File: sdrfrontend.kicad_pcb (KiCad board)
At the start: 2 copper layers, 22 parts, among them J1 AudioJack2_Ground, U1 CD4066BE, U2 NJM4580, U3 LM7805_TO220, U5 PIC12F1822-xP

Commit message: make pcb
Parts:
- C1: moved to B.Cu
- R1, R2: footprint Resistor_THT:R_Axial_DIN0207_L6.3mm_D2.5mm_P7.62mm_Horizontal -> Resistor_THT:R_Axial_DIN0207_L6.3mm_D2.5mm_P2.54mm_Vertical
- moved C5 64.6 mm to (165.1, 73.0), turned to -90 degrees
- moved C1 63.5 mm to (154.9, 102.9), turned to 90 degrees
- moved C2 61.7 mm to (162.6, 78.1), turned to -90 degrees
- moved C8 59.3 mm to (157.5, 73.0), turned to 180 degrees
- moved U2 54.2 mm to (152.4, 75.6)
- moved U1 49.0 mm to (152.4, 87.6)
- moved C3 48.8 mm to (149.9, 75.6), turned to -90 degrees
- moved R1 48.8 mm to (165.1, 80.4), turned to 90 degrees
- moved U4 48.0 mm to (142.2, 95.2)
- moved C4 47.0 mm to (147.3, 70.5), turned to -90 degrees
- moved C9 42.1 mm to (142.2, 85.7), turned to -90 degrees
- moved U5 35.9 mm to (132.1, 92.7)
- moved C7 35.8 mm to (134.6, 75.6), turned to -90 degrees
- moved C6 31.3 mm to (132.1, 80.6), turned to 90 degrees
- moved L1 31.2 mm to (149.9, 92.7), turned to 90 degrees
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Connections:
- C2 pad 2: Net-(U2A--) -> Net-(U2B--)
- C3 pad 2: Net-(U2B--) -> Net-(U2A--)
- C4 pad 2: Net-(C2-Pad1) -> Net-(C3-Pad1)
- C5 pad 2: Net-(C3-Pad1) -> Net-(C2-Pad1)
- J1 pad S: Net-(C4-Pad1) -> Net-(C5-Pad1)
- J1 pad T: Net-(C5-Pad1) -> Net-(C4-Pad1)
- R1 pad 1: Net-(U2A--) -> Net-(U2B--)
- R2 pad 1: Net-(U2B--) -> Net-(U2A--)
- U1 pad 1: Net-(C1-Pad2) -> GND
- U1 pad 13: Net-(U4-CLK2) -> GND
- U1 pad 2: Net-(U2A--) -> GND
- U1 pad 3: Net-(U2B--) -> Net-(U2A--)
- U1 pad 5: Net-(U4-CLK1) -> Net-(U4-CLK2)
- U1 pad 6: GND -> Net-(U4-CLK1)
- U1 pad 8: GND -> Net-(C1-Pad2)
- U1 pad 9: GND -> Net-(U2B--)
- U2 pad 1: Net-(C2-Pad1) -> Net-(C3-Pad1)
- U2 pad 7: Net-(C3-Pad1) -> Net-(C2-Pad1)
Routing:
- net GND: track 0.00 -> 189.7 mm, vias 0 -> 7
- net +5V: track 0.00 -> 145.7 mm
- net +2V5: track 0.00 -> 44.0 mm, vias 0 -> 2
- net Net-(C5-Pad1): track 0.00 -> 35.6 mm
- net Net-(U2B--): track 0.00 -> 27.0 mm
- net Net-(U2A--): track 0.00 -> 22.1 mm, vias 0 -> 2
- net Net-(C1-Pad2): track 0.00 -> 16.2 mm, vias 0 -> 1
- net Net-(C4-Pad1): track 0.00 -> 13.9 mm
- net Net-(C3-Pad1): track 0.00 -> 7.50 mm
- net Net-(C2-Pad1): track 0.00 -> 7.49 mm
- net Net-(D1-K): track 0.00 -> 6.99 mm
- net unconnected-(C1-Pad1): track 0.00 -> 6.97 mm
- net unconnected-(D1-A-Pad2): track 0.00 -> 3.17 mm
- net Net-(U4-SDA): track 0.00 -> 2.54 mm
- net Net-(U4-SCL): track 0.00 -> 2.54 mm
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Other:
- board outline added: 45.7 x 44.5 mm
- board text added: "+"
- board text added: "-"

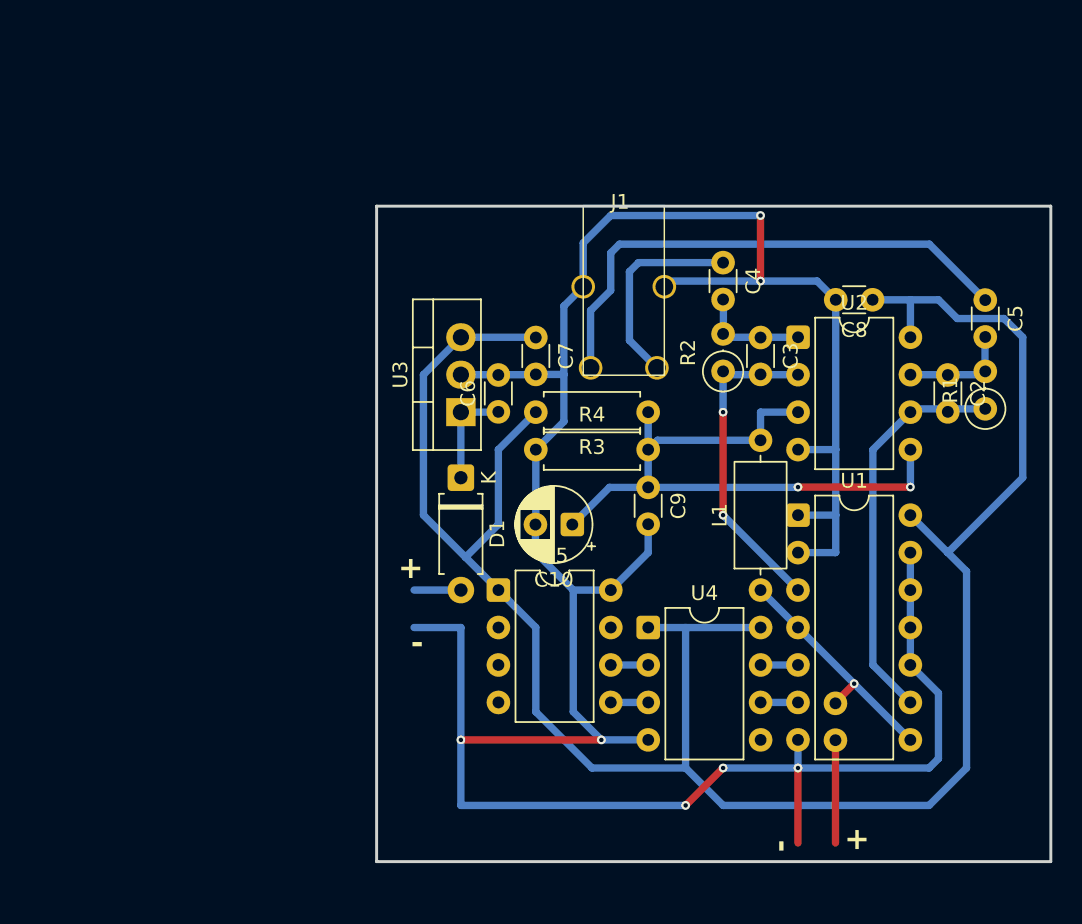
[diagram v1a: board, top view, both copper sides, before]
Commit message: add switch and sma conn
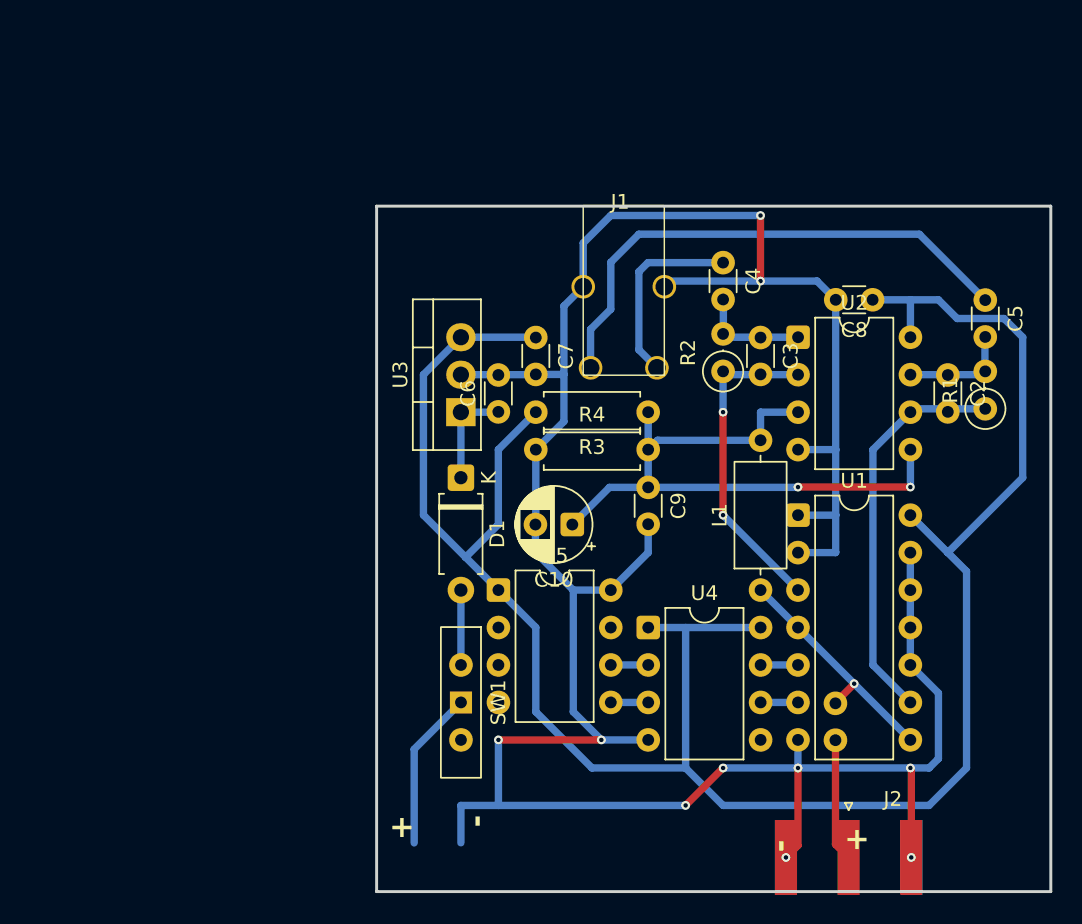
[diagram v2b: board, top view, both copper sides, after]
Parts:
- added J2: Conn_Coaxial, Connector_Coaxial:SMA_Amphenol_132289_EdgeMount, F.Cu at (155.8, 110.8)
- added SW1: SW_SPDT, Button_Switch_THT:SW_Slide-03_Wuerth-WS-SLTV_10x2.5x6.4_P2.54mm, F.Cu at (129.5, 100.3)
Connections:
- C1 pad 1: unconnected-(C1-Pad1) -> Net-(J2-In)
- D1 pad 2: unconnected-(D1-A-Pad2) -> Net-(D1-A)
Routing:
- net unconnected-(SW1-B-Pad2): track 0.00 -> 10.8 mm
- net Net-(J2-In): track 0.00 -> 8.32 mm
- net unconnected-(C1-Pad1): track 6.97 -> 0.00 mm
- net Net-(D1-A): track 0.00 -> 5.08 mm
- net GND: track 189.7 -> 186.2 mm, vias 7 -> 10
- net unconnected-(D1-A-Pad2): track 3.17 -> 0.00 mm
- net Net-(C4-Pad1): track 13.9 -> 13.0 mm
- net unconnected-(SW1-C-Pad3): vias 0 -> 1
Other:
- board size 45.7 x 44.5 mm -> 45.7 x 46.5 mm

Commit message: fix
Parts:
- moved C4 2.52 mm to (147.3, 73.0), turned to 0 degrees
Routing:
- net GND: track 186.2 -> 170.7 mm, vias 10 -> 8
- net Net-(C4-Pad1): track 13.0 -> 6.47 mm
- net Net-(C5-Pad1): track 35.8 -> 33.1 mm
- net +5V: track 145.7 -> 148.0 mm
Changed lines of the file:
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@@
 	(footprint "Capacitor_THT:C_Disc_D3.0mm_W1.6mm_P2.50mm"
 		(layer "F.Cu")
-		(at 147.315 70.505 -90)
+		(at 147.315 73.025)
 		(descr "C, Disc series, Radial, pin pitch=2.50mm, diameter*width=3.0*1.6mm^2, Capacitor, http://www.vishay.com/docs/45233/krseries.pdf")
 		(tags "C Disc series Radial pin pitch 2.50mm diameter 3.0mm width 1.6mm Capacitor")
 		(property "Reference" "C4"
-			(at 1.25 -2.05 90)
+			(at 1.25 -2.05 0)
 			(layer "F.SilkS")
 			(effects
@@
 		)
 		(property "Value" "1u"
-			(at 1.25 2.05 90)
+			(at 1.25 2.05 0)
 			(layer "F.Fab")
 			(effects
@@
 		)
 		(property "Datasheet" ""
-			(at 0 0 90)
+			(at 0 0 0)
 			(layer "F.Fab")
 			(hide yes)
@@
 		)
 		(property "Description" "Unpolarized capacitor"
-			(at 0 0 90)
+			(at 0 0 0)
 			(layer "F.Fab")
 			(hide yes)
@@
 		(attr through_hole)
 		(fp_line
-			(start 0.485 0.92)
-			(end 2.015 0.92)
+			(start 0.485 -0.92)
+			(end 2.015 -0.92)
 			(stroke
 				(width 0.12)
@@
 		)
 		(fp_line
-			(start 0.485 -0.92)
-			(end 2.015 -0.92)
+			(start 0.485 0.92)
+			(end 2.015 0.92)
 			(stroke
 				(width 0.12)
@@
 		)
 		(fp_text user "${REFERENCE}"
-			(at 1.25 0 90)
+			(at 1.25 0 0)
 			(layer "F.Fab")
 			(effects
@@
 		)
 		(pad "1" thru_hole circle
-			(at 0 0 270)
+			(at 0 0)
 			(size 1.6 1.6)
 			(drill 0.8)
@@
 		)
 		(pad "2" thru_hole circle
-			(at 2.5 0 270)
+			(at 2.5 0)
 			(size 1.6 1.6)
 			(drill 0.8)
@@
 	)
 	(segment
-		(start 147.335 73.025)
-		(end 147.335 75.32)
+		(start 149.815 73.025)
+		(end 149.815 75.545)
 		(width 0.5)
 		(layer "B.Cu")
@@
 	)
 	(segment
+		(start 149.815 75.545)
+		(end 149.855 75.585)
+		(width 0.5)
+		(layer "B.Cu")
+		(net 4)
+	)
+	(segment
 		(start 147.335 75.32)
 		(end 147.315 75.34)
@@
 	)
 	(segment
-		(start 142.83 77.64)
-		(end 141.605 76.415)
+		(start 147.315 73.025)
+		(end 142.83 77.51)
 		(width 0.5)
 		(layer "B.Cu")
@@
 	)
 	(segment
-		(start 141.605 71.12)
-		(end 142.22 70.505)
+		(start 142.83 77.51)
+		(end 142.83 77.64)
 		(width 0.5)
 		(layer "B.Cu")
@@
 	)
 	(segment
-		(start 141.605 76.415)
-		(end 141.605 71.12)
-		(width 0.5)
-		(layer "B.Cu")
-		(net 6)
-	)
-	(segment
-		(start 142.22 70.505)
-		(end 147.315 70.505)
-		(width 0.5)
-		(layer "B.Cu")
-		(net 6)
-	)
-	(segment
-		(start 139.7 70.485)
-		(end 139.7 73.66)
+		(start 165.095 73.045)
+		(end 162.535 70.485)
 		(width 0.5)
 		(layer "B.Cu")
@@
 	)
 	(segment
-		(start 139.7 73.66)
-		(end 138.33 75.03)
+		(start 138.33 77.57)
+		(end 138.33 77.64)
 		(width 0.5)
 		(layer "B.Cu")
@@
 	)
 	(segment
-		(start 165.095 73.045)
-		(end 160.63 68.58)
+		(start 162.535 70.485)
+		(end 141.605 70.485)
 		(width 0.5)
 		(layer "B.Cu")
@@
 	)
 	(segment
-		(start 160.63 68.58)
-		(end 141.605 68.58)
+		(start 141.605 70.485)
+		(end 140.335 71.755)
 		(width 0.5)
 		(layer "B.Cu")
@@
 	)
 	(segment
-		(start 141.605 68.58)
-		(end 139.7 70.485)
+		(start 140.335 75.565)
+		(end 138.33 77.57)
 		(width 0.5)
 		(layer "B.Cu")
@@
 	)
 	(segment
-		(start 138.33 75.03)
-		(end 138.33 77.64)
+		(start 140.335 71.755)
+		(end 140.335 75.565)
 		(width 0.5)
 		(layer "B.Cu")
@@
 	)
 	(segment
-		(start 144.775 107.315)
-		(end 147.315 104.775)
+		(start 132.08 102.87)
+		(end 137.16 102.87)
 		(width 0.5)
 		(layer "F.Cu")
@@
 	)
 	(segment
-		(start 139.06 102.87)
-		(end 132.08 102.87)
+		(start 143.33 72.14)
+		(end 137.83 72.14)
 		(width 0.5)
 		(layer "F.Cu")
@@
 	)
 	(segment
-		(start 149.855 71.755)
-		(end 149.855 67.31)
+		(start 144.775 107.315)
+		(end 147.315 104.775)
 		(width 0.5)
 		(layer "F.Cu")
@@
 	)
 	(via
-		(at 149.855 71.755)
-		(size 0.6)
-		(drill 0.3)
-		(layers "F.Cu" "B.Cu")
-		(net 9)
-	)
-	(via
 		(at 144.775 107.315)
 		(size 0.6)
@@
 	)
 	(via
-		(at 149.855 67.31)
+		(at 137.16 102.87)
 		(size 0.6)
 		(drill 0.3)
@@
 		(net 9)
 	)
-	(via
-		(at 139.06 102.87)
-		(size 0.6)
-		(drill 0.3)
-		(layers "F.Cu" "B.Cu")
-		(net 9)
-	)
 	(segment
 		(start 152.395 104.775)
@@
 	)
 	(segment
-		(start 137.155 100.965)
-		(end 137.155 92.71)
-		(width 0.5)
-		(layer "B.Cu")
-		(net 9)
-	)
-	(segment
 		(start 139.7 92.71)
 		(end 139.7 92.705)
@@
 	)
 	(segment
-		(start 137.83 69.175)
-		(end 137.83 72.14)
-		(width 0.5)
-		(layer "B.Cu")
-		(net 9)
-	)
-	(segment
-		(start 139.06 102.87)
-		(end 137.155 100.965)
+		(start 137.155 102.865)
+		(end 137.155 92.71)
 		(width 0.5)
 		(layer "B.Cu")
@@
 	)
 	(segment
-		(start 142.24 102.87)
-		(end 139.06 102.87)
-		(width 0.5)
-		(layer "B.Cu")
-		(net 9)
-	)
-	(segment
 		(start 161.285 104.775)
 		(end 161.92 104.14)
@@
 	)
 	(segment
-		(start 149.855 67.31)
-		(end 139.695 67.31)
+		(start 142.24 102.87)
+		(end 137.16 102.87)
 		(width 0.5)
 		(layer "B.Cu")
@@
 	)
 	(segment
+		(start 137.16 102.87)
+		(end 137.155 102.865)
+		(width 0.5)
+		(layer "B.Cu")
+		(net 9)
+	)
+	(segment
 		(start 152.395 87.63)
 		(end 154.955 87.63)
@@
 	)
 	(segment
-		(start 139.695 67.31)
-		(end 137.83 69.175)
-		(width 0.5)
-		(layer "B.Cu")
-		(net 9)
-	)
-	(segment
-		(start 134.615 95.245)
-		(end 134.615 100.965)
-		(width 0.5)
-		(layer "B.Cu")
-		(net 10)
-	)
-	(segment
 		(start 134.615 80.645)
 		(end 132.075 83.185)
@@
 	)
 	(segment
+		(start 134.62 104.775)
+		(end 144.775 104.775)
+		(width 0.5)
+		(layer "B.Cu")
+		(net 10)
+	)
+	(segment
 		(start 149.86 95.25)
 		(end 144.775 95.25)
@@
 	)
 	(segment
+		(start 134.615 104.77)
+		(end 134.62 104.775)
+		(width 0.5)
+		(layer "B.Cu")
+		(net 10)
+	)
+	(segment
 		(start 166.365 74.295)
 		(end 163.19 74.295)
@@
 	)
 	(segment
-		(start 132.08 92.71)
-		(end 134.615 95.245)
+		(start 167.635 75.565)
+		(end 166.365 74.295)
 		(width 0.5)
 		(layer "B.Cu")
@@
 	)
 	(segment
-		(start 167.635 75.565)
-		(end 166.365 74.295)
+		(start 144.775 104.775)
+		(end 144.775 95.25)
 		(width 0.5)
 		(layer "B.Cu")
@@
 	)
 	(segment
-		(start 144.775 104.775)
-		(end 144.775 95.25)
+		(start 134.615 95.245)
+		(end 134.615 104.77)
 		(width 0.5)
 		(layer "B.Cu")
@@
 	)
 	(segment
-		(start 162.555 90.17)
-		(end 163.825 91.44)
-		(width 0.5)
-		(layer "B.Cu")
-		(net 10)
-	)
-	(segment
-		(start 167.635 85.09)
-		(end 167.635 75.565)
+		(start 132.08 92.71)
+		(end 134.615 95.245)
 		(width 0.5)
 		(layer "B.Cu")
@@
 	)
 	(segment
-		(start 138.425 104.775)
-		(end 144.775 104.775)
+		(start 162.555 90.17)
+		(end 163.825 91.44)
 		(width 0.5)
 		(layer "B.Cu")
@@
 	)
 	(segment
-		(start 134.615 100.965)
-		(end 138.425 104.775)
+		(start 167.635 85.09)
+		(end 167.635 75.565)
 		(width 0.5)
 		(layer "B.Cu")
